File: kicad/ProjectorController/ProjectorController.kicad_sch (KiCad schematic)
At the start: 16 parts, among them J1 ISP, J2 Keypad, J3 Switch, J4 Keypad, U1 MAX232, U2 ATmega48-20P

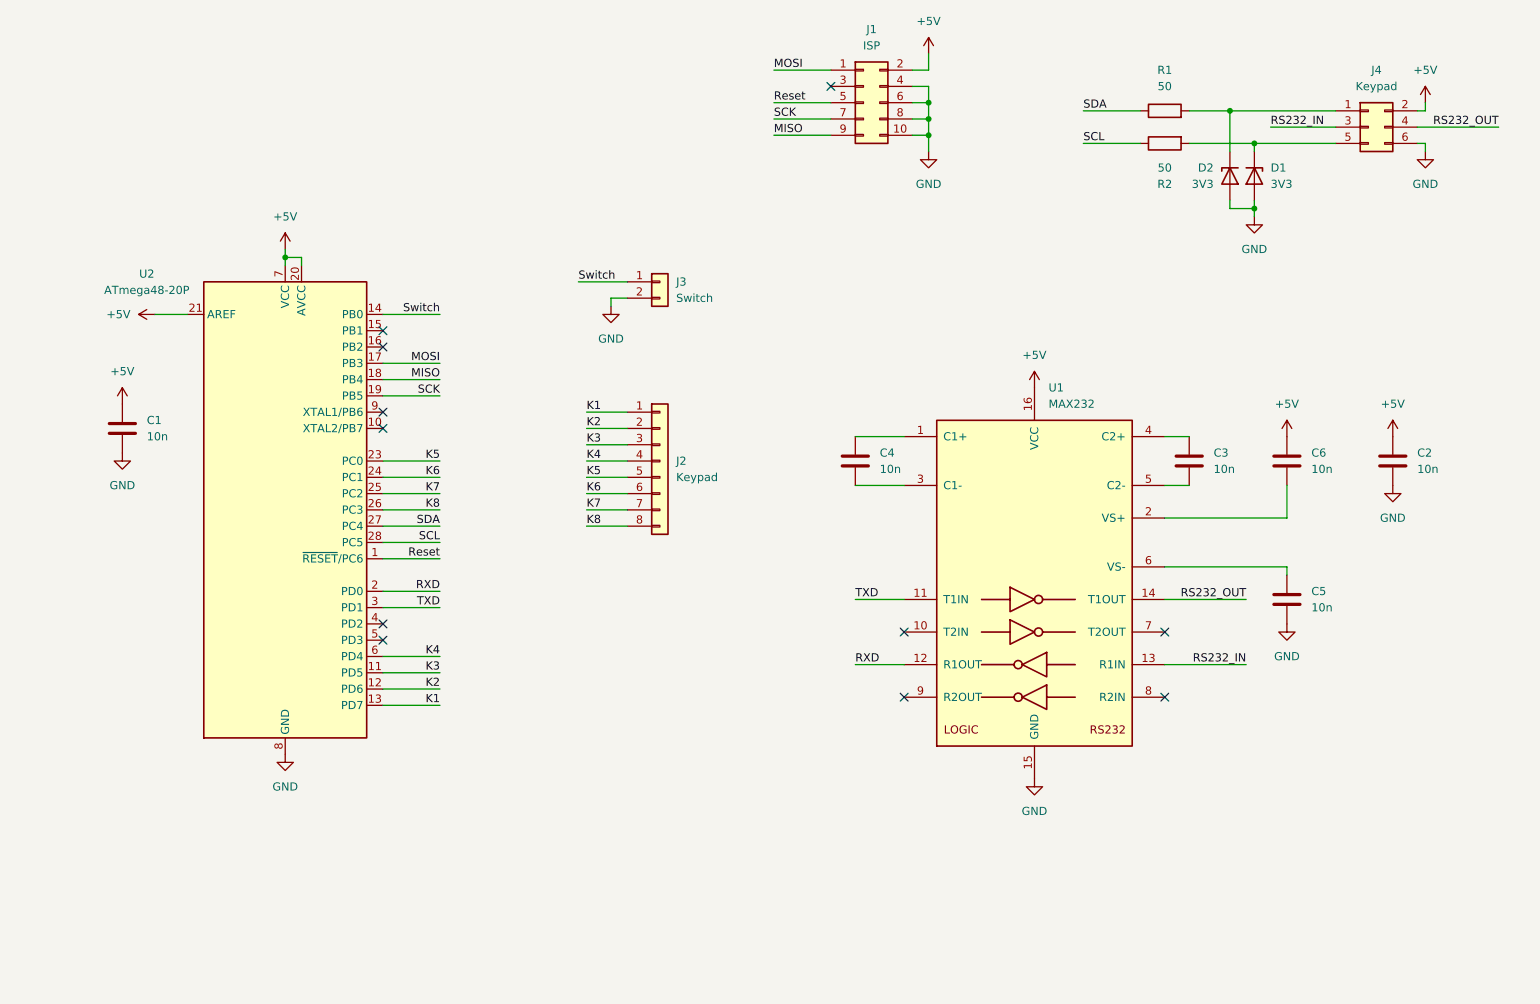
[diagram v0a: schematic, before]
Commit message: Added schematics for projector controller, initial source project
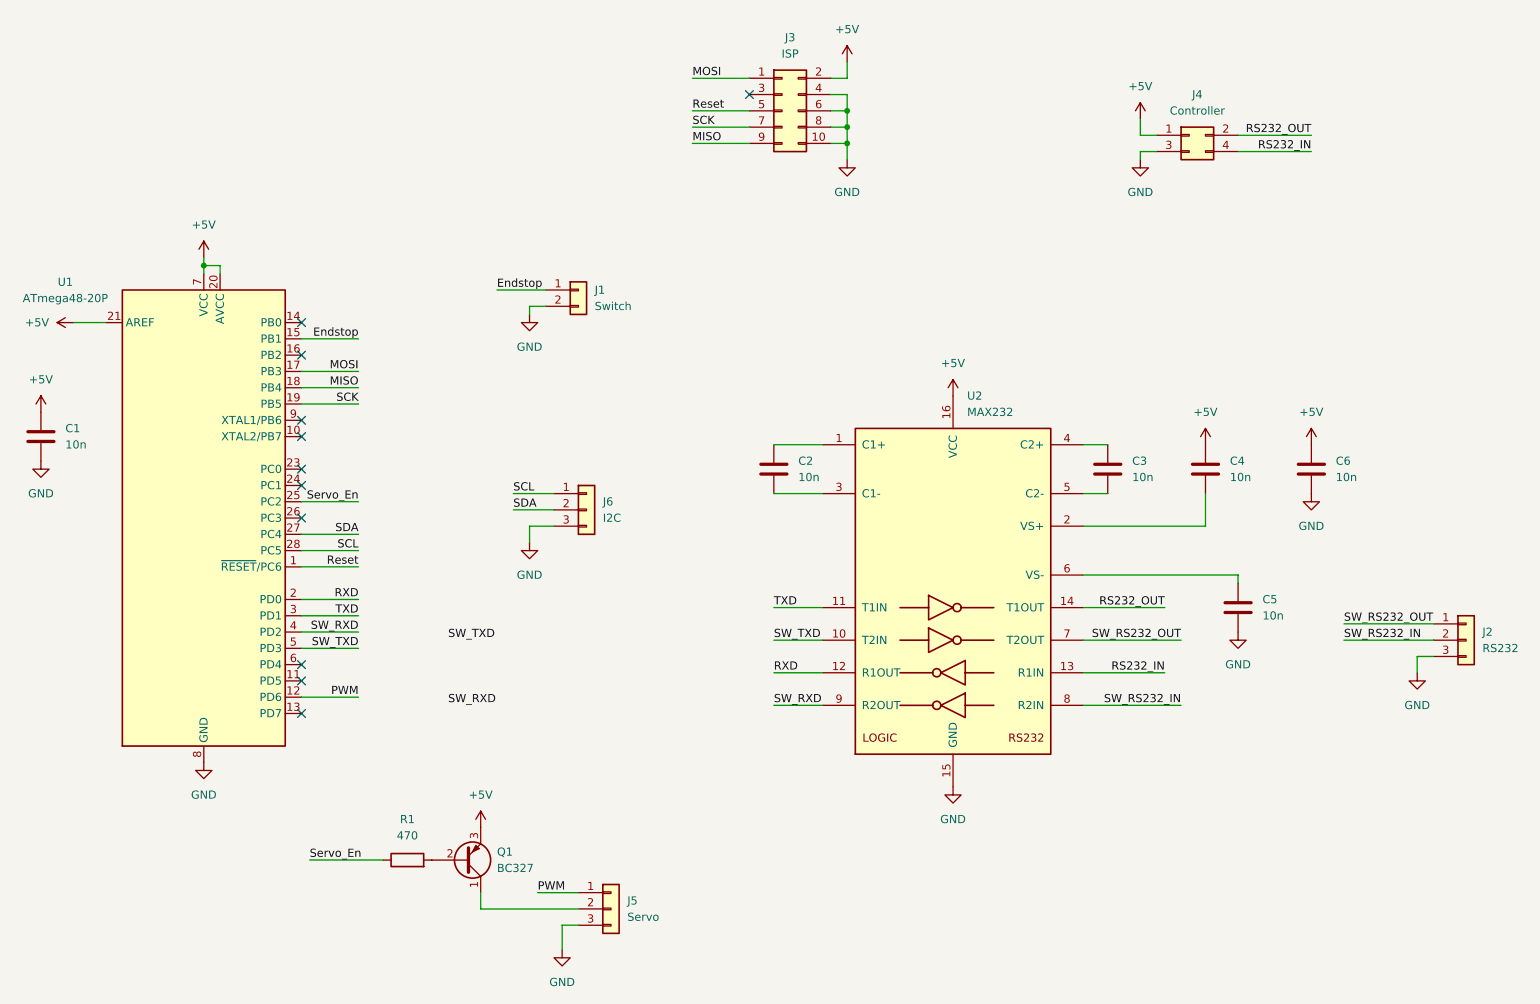
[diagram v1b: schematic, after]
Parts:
- removed D1, D2: 3V3, Diode_THT:D_DO-34_SOD68_P7.62mm_Horizontal, symbol Device:D_Zener
- removed J1: ISP, Connector_IDC:IDC-Header_2x05_P2.54mm_Horizontal, symbol Connector_Generic:Conn_02x05_Odd_Even
- removed J2: Keypad, Connector_PinHeader_1.00mm:PinHeader_1x08_P1.00mm_Horizontal, symbol Connector_Generic:Conn_01x08
- removed J3: Switch, Connector_PinHeader_1.00mm:PinHeader_1x02_P1.00mm_Horizontal, symbol Connector_Generic:Conn_01x02
- removed J4: Keypad, symbol Connector_Generic:Conn_02x03_Odd_Even
- removed R2: 50, Resistor_THT:R_Axial_DIN0204_L3.6mm_D1.6mm_P2.54mm_Vertical, symbol Device:R
- removed U1: MAX232, Package_DIP:DIP-16_W7.62mm, symbol Interface_UART:MAX232
- removed U2: ATmega48-20P, Package_DIP:DIP-28_W7.62mm, symbol MCU_Microchip_ATmega:ATmega48-20P
- added J1: Switch, Connector_PinHeader_1.00mm:PinHeader_1x02_P1.00mm_Horizontal, symbol Connector_Generic:Conn_01x02
- added J2: RS232, symbol Connector_Generic:Conn_01x03
- added J3: ISP, Connector_IDC:IDC-Header_2x05_P2.54mm_Horizontal, symbol Connector_Generic:Conn_02x05_Odd_Even
- added J4: Controller, symbol Connector_Generic:Conn_02x02_Odd_Even
- added J5: Servo, symbol Connector_Generic:Conn_01x03
- added J6: I2C, symbol Connector_Generic:Conn_01x03
- added Q1: BC327, Package_TO_SOT_THT:TO-92_Inline, symbol Transistor_BJT:BC327
- added U1: ATmega48-20P, Package_DIP:DIP-28_W7.62mm, symbol MCU_Microchip_ATmega:ATmega48-20P
- added U2: MAX232, Package_DIP:DIP-16_W7.62mm, symbol Interface_UART:MAX232
- R1: value 50 -> 470
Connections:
- net +5V: now also C4.2, C6.1, J3.2 (Pin_2), J4.1 (Pin_1), Q1.3 (E), U1.20 (AVCC), U1.21 (AREF), U1.7 (VCC), U2.16 (VCC); no longer C2.1, C6.2
- net GND: now also C6.2, J1.2 (Pin_2), J2.3 (Pin_3), J3.10 (Pin_10), J3.4 (Pin_4), J3.6 (Pin_6), J3.8 (Pin_8), J4.3 (Pin_3), J5.3 (Pin_3), J6.3 (Pin_3), U1.22 (GND), U1.8 (GND), U2.15 (GND); no longer C2.2
- net MISO: now also J3.9 (Pin_9), U1.18 (PB4)
- net MOSI: now also J3.1 (Pin_1), U1.17 (PB3)
- net RS232_IN: now also J4.4 (Pin_4), U2.13 (R1IN)
- net RS232_OUT: now also J4.2 (Pin_2), U2.14 (T1OUT)
- net RXD: now also U1.2 (PD0), U2.12 (R1OUT)
- net Reset: now also J3.5 (Pin_5), U1.1 (~{RESET}/PC6)
- net SCK: now also J3.7 (Pin_7), U1.19 (PB5)
- net SCL: now also J6.1 (Pin_1), U1.28 (PC5)
- net SDA: now also J6.2 (Pin_2), U1.27 (PC4); no longer R1.1
- net TXD: now also U1.3 (PD1), U2.11 (T1IN)
- net at C4.1: now also U2.2 (VS+)
- net at C5.1: now also U2.6 (VS-)
- net at C3.1: now also U2.4 (C2+)
- net at C3.2: now also U2.5 (C2-)
- net at R1.2: now also Q1.2 (B)
- new net: C2.1, U2.1 (C1+)
- new net: C2.2, U2.3 (C1-)
- new net: J5.2 (Pin_2), Q1.1 (C)
- new net Endstop: J1.1 (Pin_1), U1.15 (PB1)
- new net PWM: J5.1 (Pin_1), U1.12 (PD6)
- new net SW_RS232_IN: J2.2 (Pin_2), U2.8 (R2IN)
- new net SW_RS232_OUT: J2.1 (Pin_1), U2.7 (T2OUT)
- new net SW_RXD: U1.4 (PD2), U2.9 (R2OUT)
- new net SW_TXD: U1.5 (PD3), U2.10 (T2IN)
- new net Servo_En: R1.1, U1.25 (PC2)

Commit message: Complete schematics, using UART for communications
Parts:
- removed J6: I2C, symbol Connector_Generic:Conn_01x03
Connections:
- net RS232_IN: now also U2.8 (R2IN); no longer U2.13 (R1IN)
- net RS232_OUT: now also U2.7 (T2OUT); no longer U2.14 (T1OUT)
- net RXD: now also U2.9 (R2OUT); no longer U2.12 (R1OUT)
- net SW_RS232_IN: now also U2.13 (R1IN); no longer U2.8 (R2IN)
- net SW_RS232_OUT: now also U2.14 (T1OUT); no longer U2.7 (T2OUT)
- net SW_RXD: now also U2.12 (R1OUT); no longer U2.9 (R2OUT)
- net SW_TXD: now also U2.11 (T1IN); no longer U2.10 (T2IN)
- net TXD: now also U2.10 (T2IN); no longer U2.11 (T1IN)
- net SCL: no longer names the net of U1.28 (PC5)
- net SDA: no longer names the net of U1.27 (PC4)
- no-connect marks 11 -> 13
